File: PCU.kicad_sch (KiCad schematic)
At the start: 1 part, among them U2 EPC2152ENGRT

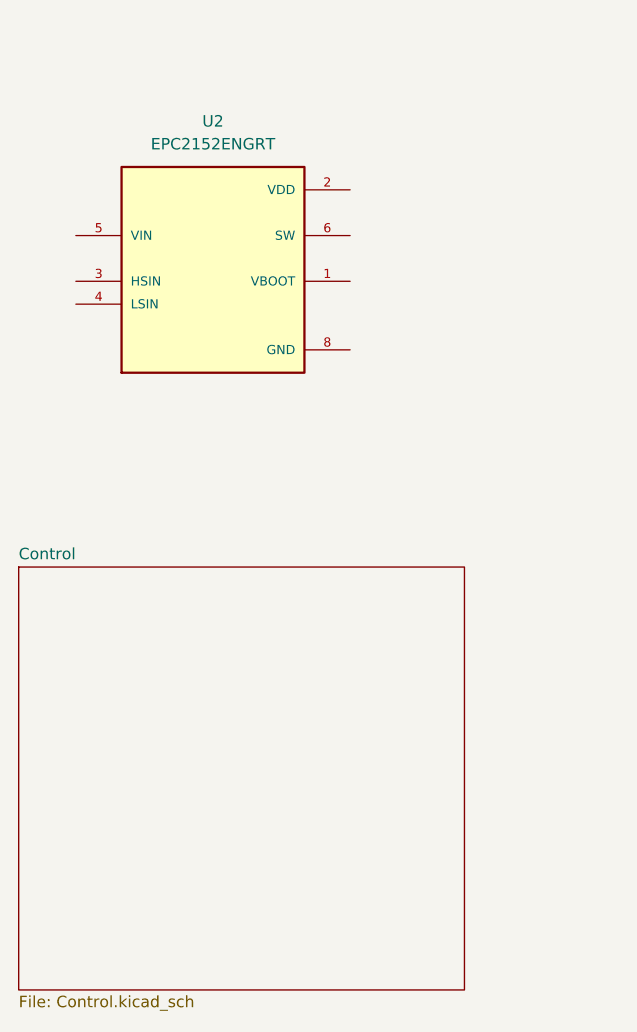
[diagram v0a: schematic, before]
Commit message: changed epc gan symbol
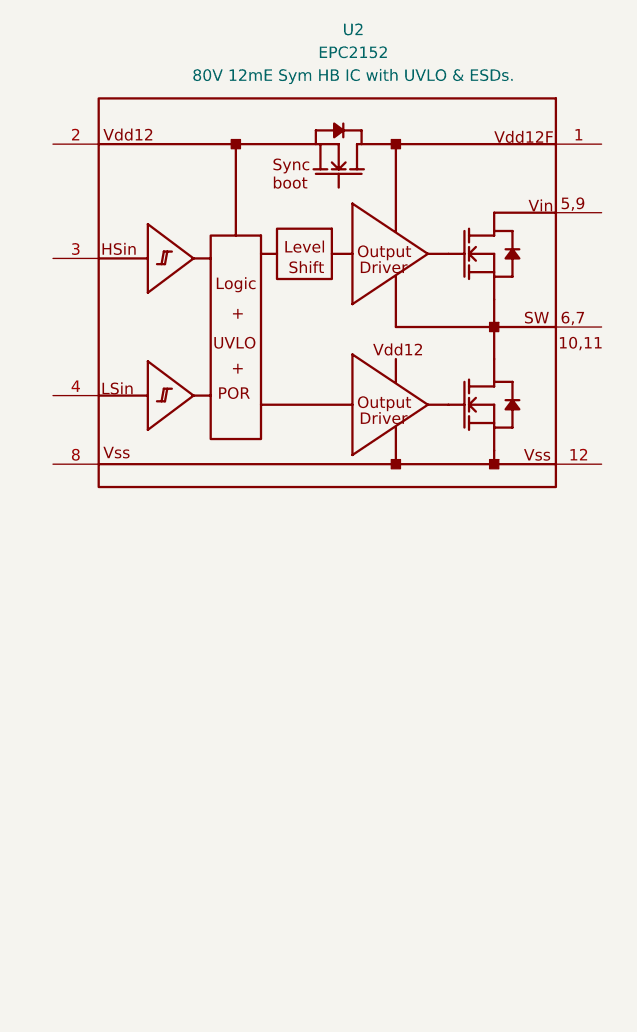
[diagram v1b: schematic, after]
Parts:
- removed U2: EPC2152ENGRT, PULSE_Library:VREG_EPC2152ENGRT, symbol PULSE_Library:EPC2152ENGRT
- added U2: EPC2152, PULSE_Library:D0122, symbol PULSE_Library:EPC2152
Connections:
- new net: U2.10 (SW), U2.11 (SW), U2.6 (SW), U2.7 (SW)
- new net: U2.5 (Vin), U2.9 (Vin)
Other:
- removed sheet Control
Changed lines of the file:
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@@
 	)
 	(symbol
-		(lib_id "PULSE_Library:EPC2152ENGRT")
-		(at 106.68 77.47 0)
+		(lib_id "PULSE_Library:EPC2152")
+		(at 93.98 102.87 0)
 		(unit 1)
 		(exclude_from_sim no)
@@
 		(fields_autoplaced yes)
 		(property "Reference" "U2"
-			(at 106.68 62.23 0)
+			(at 122.2761 52.07 0)
 			(effects
 				(font
@@
 			)
 		)
-		(property "Value" "EPC2152ENGRT"
-			(at 106.68 64.77 0)
+		(property "Value" "EPC2152"
+			(at 122.2761 54.61 0)
 			(effects
 				(font
@@
 			)
 		)
-		(property "Footprint" "PULSE_Library:VREG_EPC2152ENGRT"
-			(at 106.68 77.47 0)
-			(effects
-				(font
-					(size 1.27 1.27)
-				)
-				(justify bottom)
-				(hide yes)
-			)
-		)
-		(property "Datasheet" "https://epc-co.com/epc/portals/0/epc/documents/datasheets/EPC2152_datasheet.pdf"
-			(at 106.68 77.47 0)
+		(property "Footprint" "PULSE_Library:D0122"
+			(at 108.3564 56.2356 0)
 			(effects
 				(font
@@
 			)
 		)
-		(property "Description" "ePower™ Stage IC"
-			(at 106.68 77.47 0)
+		(property "Datasheet" ""
+			(at 93.98 102.87 0)
 			(effects
 				(font
@@
 			)
 		)
-		(property "MF" "EPC"
-			(at 106.68 77.47 0)
+		(property "Description" "80V 12mE Sym HB IC with UVLO & ESDs."
+			(at 122.2761 57.15 0)
 			(effects
 				(font
 					(size 1.27 1.27)
 				)
-				(justify bottom)
-				(hide yes)
 			)
 		)
-		(property "MAXIMUM_PACKAGE_HEIGHT" "0.842mm"
-			(at 106.68 77.47 0)
-			(effects
-				(font
-					(size 1.27 1.27)
-				)
-				(justify bottom)
-				(hide yes)
-			)
-		)
-		(property "Package" "WFLGA-12 EPC"
-			(at 106.68 77.47 0)
-			(effects
-				(font
-					(size 1.27 1.27)
-				)
-				(justify bottom)
-				(hide yes)
-			)
-		)
-		(property "Price" "None"
-			(at 106.68 77.47 0)
-			(effects
-				(font
-					(size 1.27 1.27)
-				)
-				(justify bottom)
-				(hide yes)
-			)
-		)
-		(property "Check_prices" "https://www.snapeda.com/parts/EPC2152ENGRT/EPC/view-part/?ref=eda"
-			(at 106.68 77.47 0)
-			(effects
-				(font
-					(size 1.27 1.27)
-				)
-				(justify bottom)
-				(hide yes)
-			)
-		)
-		(property "STANDARD" "Manufacturer Recommendations"
-			(at 106.68 77.47 0)
-			(effects
-				(font
-					(size 1.27 1.27)
-				)
-				(justify bottom)
-				(hide yes)
-			)
-		)
-		(property "PARTREV" "2.0"
-			(at 106.68 77.47 0)
-			(effects
-				(font
-					(size 1.27 1.27)
-				)
-				(justify bottom)
-				(hide yes)
-			)
-		)
-		(property "SnapEDA_Link" "https://www.snapeda.com/parts/EPC2152ENGRT/EPC/view-part/?ref=snap"
-			(at 106.68 77.47 0)
-			(effects
-				(font
-					(size 1.27 1.27)
-				)
-				(justify bottom)
-				(hide yes)
-			)
-		)
-		(property "MP" "EPC2152ENGRT"
-			(at 106.68 77.47 0)
-			(effects
-				(font
-					(size 1.27 1.27)
-				)
-				(justify bottom)
-				(hide yes)
-			)
-		)
-		(property "Description_1" "Half Bridge Driver Synchronous Buck Converters Gallium Nitride (GaN) FETs 12-LGA (3.85x2.59)"
-			(at 106.68 77.47 0)
-			(effects
-				(font
-					(size 1.27 1.27)
-				)
-				(justify bottom)
-				(hide yes)
-			)
-		)
-		(property "Availability" "In Stock"
-			(at 106.68 77.47 0)
-			(effects
-				(font
-					(size 1.27 1.27)
-				)
-				(justify bottom)
-				(hide yes)
-			)
-		)
-		(property "MANUFACTURER" "EPC"
-			(at 106.68 77.47 0)
-			(effects
-				(font
-					(size 1.27 1.27)
-				)
-				(justify bottom)
-				(hide yes)
-			)
-		)
-		(pin "12"
-		)
-		(pin "1"
-		)
-		(pin "7"
-		)
-		(pin "6"
-		)
-		(pin "11"
-		)
-		(pin "10"
-		)
-		(pin "2"
+		(pin "8"
 		)
 		(pin "4"
@@
 		(pin "3"
 		)
-		(pin "9"
+		(pin "2"
+		)
+		(pin "6"
+		)
+		(pin "12"
+		)
+		(pin "7"
+		)
+		(pin "1"
 		)
 		(pin "5"
 		)
-		(pin "8"
+		(pin "10"
+		)
+		(pin "9"
+		)
+		(pin "11"
 		)
 		(instances
@@
 				)
 			)
-		)
-	)
-	(sheet
-		(at 85.09 111.76)
-		(size 49.53 46.99)
-		(exclude_from_sim no)
-		(in_bom yes)
-		(on_board yes)
-		(dnp no)
-		(fields_autoplaced yes)
-		(stroke
-			(width 0.1524)
-			(type solid)
-		)
-		(fill
-			(color 0 0 0 0.0000)
-		)
-		(property "Sheetname" "Control"
-			(at 85.09 111.0484 0)
-			(effects
-				(font
-					(size 1.27 1.27)
-				)
-				(justify left bottom)
-			)
-		)
-		(property "Sheetfile" "Control.kicad_sch"
-			(at 85.09 159.3346 0)
-			(effects
-				(font
-					(size 1.27 1.27)
-				)
-				(justify left top)
-			)
-		)
-		(instances
-			(project "PULSE_ENG"
-				(path "/2de881bb-2e2a-47f9-96ed-b3393fa36b98/32fac869-3c72-4ec8-a514-1800b5db5371"
-					(page "5")
-				)
-			)

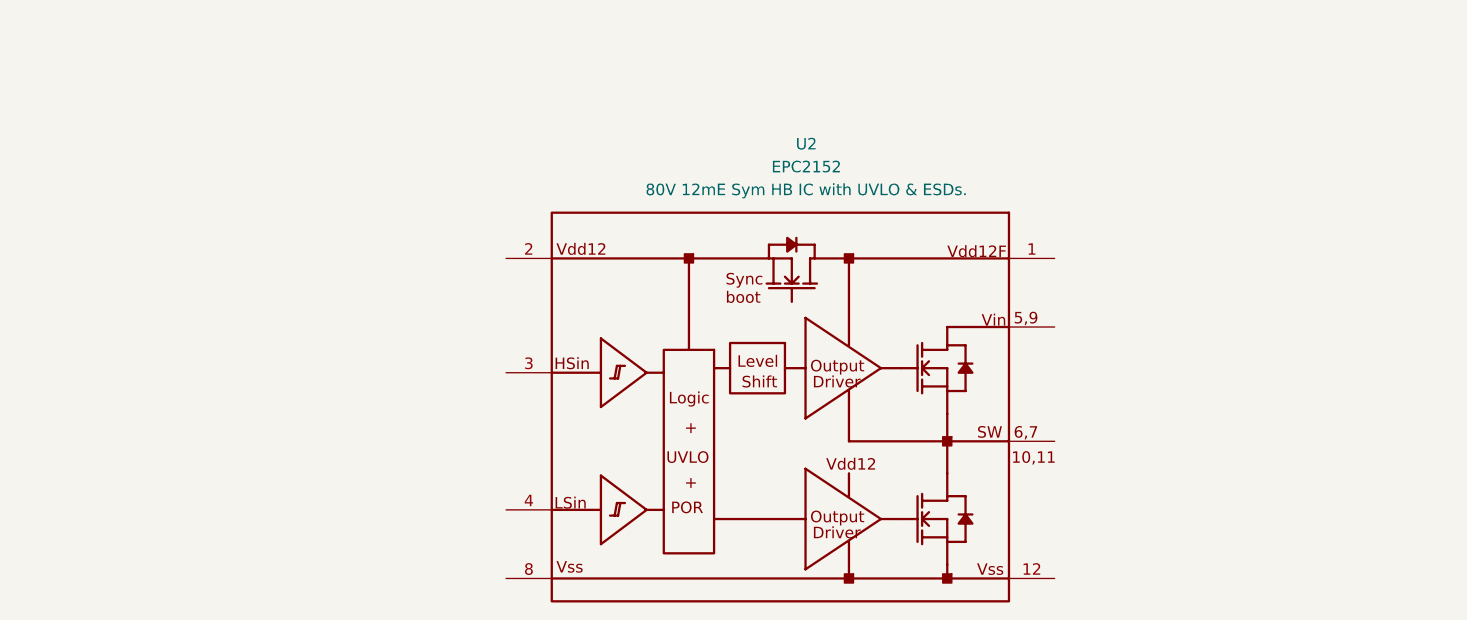
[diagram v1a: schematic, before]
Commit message: Add PCU buck converter section and notebook link
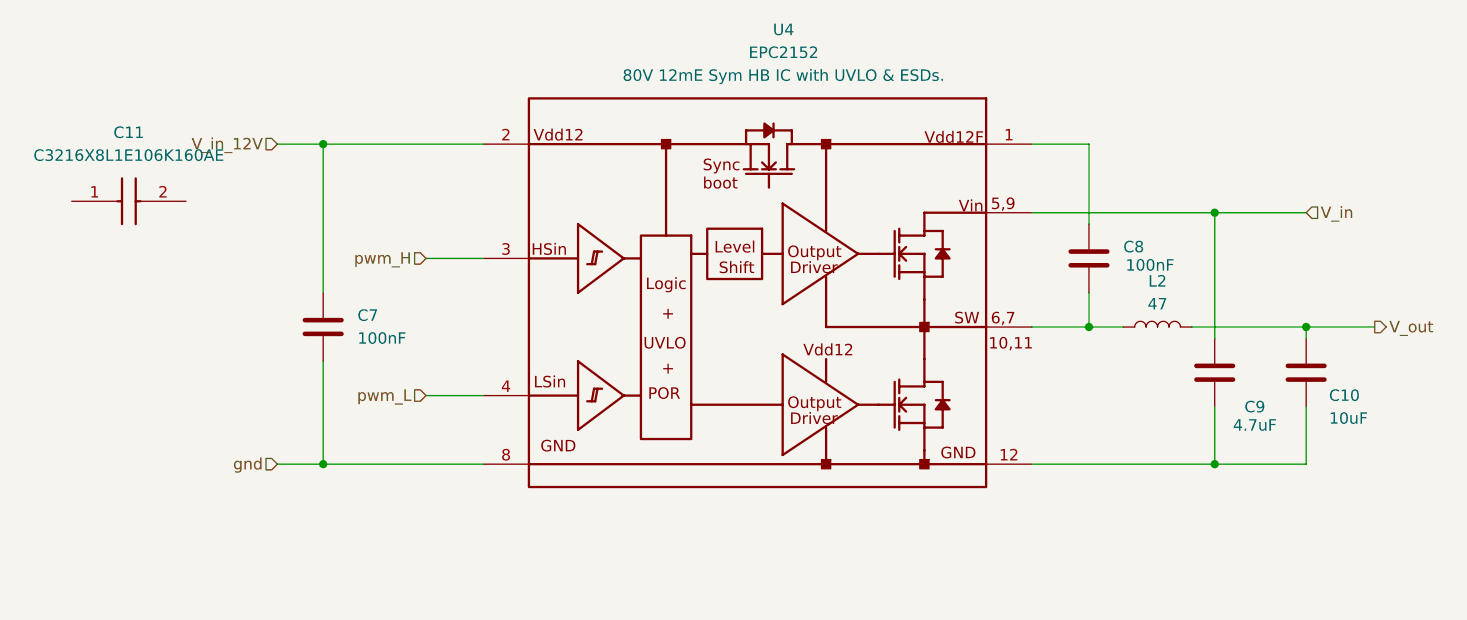
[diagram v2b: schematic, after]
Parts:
- removed U2: EPC2152, PULSE_Library:D0122, symbol PULSE_Library:EPC2152
- added C10: 10uF, symbol SamacSys_Parts:C
- added C11: C3216X8L1E106K160AE, CAPC3216X180N, symbol PULSE_Library:C3216X8L1E106K160AE
- added C7, C8: 100nF, symbol SamacSys_Parts:C
- added C9: 4.7uF, symbol SamacSys_Parts:C
- added L2: 47, symbol SamacSys_Parts:L
- added U4: EPC2152, EPC_FETs:D0122, symbol SamacSys_Parts:EPC2152
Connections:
- new net: C10.2, C9.2, U4.12 (Vss)
- new net: C8.1, U4.1 (Vdd12F)
- new net: C8.2, L2.1, U4.10 (SW), U4.11 (SW), U4.6 (SW), U4.7 (SW)
- new net V_in: C9.1, U4.5 (Vin), U4.9 (Vin)
- new net V_in_12V: C7.2, U4.2 (Vdd12)
- new net V_out: C10.1, L2.2
- new net gnd: C7.1, U4.8 (Vss)
- new net pwm_H: U4.3 (HSin)
- new net pwm_L: U4.4 (LSin)

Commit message: buck
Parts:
- removed C10: 10uF, symbol SamacSys_Parts:C
- removed C11: C3216X8L1E106K160AE, CAPC3216X180N, symbol PULSE_Library:C3216X8L1E106K160AE
- added C12: C3216X8L1E106K160AE, CAPC3216X180N, symbol PULSE_Library:C3216X8L1E106K160AE
- added Y1: AMDLA4020S-220MT, PULSE_Library:INDPM4440X200N, symbol PULSE_Library:AMDLA4020S-220MT
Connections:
- net V_out: now also C12.2
- net at C9.2, U4.12 (Vss): now also C12.1
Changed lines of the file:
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@@
+	)
+	(junction
+		(at 177.8 72.39)
+		(diameter 0)
+		(color 0 0 0 0)
 	)
 	(junction
@@
 		(color 0 0 0 0)
 	)
-	(junction
-		(at 177.8 72.39)
-		(diameter 0)
-		(color 0 0 0 0)
-	)
-	(wire
-		(pts
-			(xy 177.8 81.28) (xy 177.8 87.63)
+	(wire
+		(pts
+			(xy 177.8 72.39) (xy 185.42 72.39)
 		)
 		(stroke
@@
 	(wire
 		(pts
-			(xy 177.8 73.66) (xy 177.8 72.39)
-		)
-		(stroke
-			(width 0)
-			(type default)
-		)
-	)
-	(wire
-		(pts
 			(xy 153.67 72.39) (xy 157.48 72.39)
 		)
@@
 	(wire
 		(pts
-			(xy 177.8 72.39) (xy 185.42 72.39)
-		)
-		(stroke
-			(width 0)
-			(type default)
-		)
-	)
-	(wire
-		(pts
 			(xy 68.58 68.58) (xy 68.58 52.07)
 		)
@@
 		(pts
 			(xy 153.67 52.07) (xy 153.67 60.96)
+		)
+		(stroke
+			(width 0)
+			(type default)
+		)
+	)
+	(wire
+		(pts
+			(xy 177.8 74.93) (xy 177.8 72.39)
 		)
 		(stroke
@@
 	)
 	(symbol
-		(lib_id "SamacSys_Parts:C")
-		(at 177.8 77.47 0)
-		(unit 1)
-		(exclude_from_sim no)
-		(in_bom yes)
-		(on_board yes)
-		(dnp no)
-		(property "Reference" "C10"
-			(at 180.34 80.01 0)
-			(effects
-				(font
-					(size 1.27 1.27)
-				)
-				(justify left)
-			)
-		)
-		(property "Value" "10uF"
-			(at 180.34 82.55 0)
-			(effects
-				(font
-					(size 1.27 1.27)
-				)
-				(justify left)
-			)
-		)
-		(property "Footprint" ""
-			(at 178.7652 81.28 0)
-			(effects
-				(font
-					(size 1.27 1.27)
-				)
-				(hide yes)
-			)
-		)
-		(property "Datasheet" "~"
-			(at 177.8 77.47 0)
-			(effects
-				(font
-					(size 1.27 1.27)
-				)
-				(hide yes)
-			)
-		)
-		(property "Description" "Unpolarized capacitor"
-			(at 177.8 77.47 0)
-			(effects
-				(font
-					(size 1.27 1.27)
-				)
-				(hide yes)
-			)
-		)
-		(pin "2"
-		)
-		(pin "1"
-		)
-		(instances
-			(project "PULSE_ENG"
-				(path "/2de881bb-2e2a-47f9-96ed-b3393fa36b98/32fac869-3c72-4ec8-a514-1800b5db5371"
-					(reference "C10")
-					(unit 1)
-				)
-			)
-		)
-	)
-	(symbol
 		(lib_id "PULSE_Library:C3216X8L1E106K160AE")
-		(at 40.64 58.42 0)
+		(at 177.8 87.63 90)
 		(unit 1)
 		(exclude_from_sim no)
@@
 		(dnp no)
 		(fields_autoplaced yes)
-		(property "Reference" "C11"
-			(at 46.99 50.8 0)
-			(effects
-				(font
-					(size 1.27 1.27)
-				)
+		(property "Reference" "C12"
+			(at 181.61 80.0099 90)
+			(effects
+				(font
+					(size 1.27 1.27)
+				)
+				(justify right)
 			)
 		)
 		(property "Value" "C3216X8L1E106K160AE"
-			(at 46.99 53.34 0)
-			(effects
-				(font
-					(size 1.27 1.27)
-				)
+			(at 181.61 82.5499 90)
+			(effects
+				(font
+					(size 1.27 1.27)
+				)
+				(justify right)
 			)
 		)
 		(property "Footprint" "CAPC3216X180N"
-			(at 49.53 154.61 0)
+			(at 273.99 78.74 0)
 			(effects
 				(font
@@
 		)
 		(property "Datasheet" "https://product.tdk.com/info/en/catalog/datasheets/mlcc_commercial_midvoltage_en.pdf"
-			(at 49.53 254.61 0)
+			(at 373.99 78.74 0)
 			(effects
 				(font
@@
 		)
 		(property "Description" "MULTILAYER CERAMIC CHIP CAPACITORS, 3216, Commercial grade, general (Up to 75V)"
-			(at 40.64 58.42 0)
+			(at 177.8 87.63 0)
 			(effects
 				(font
@@
 		)
 		(property "Height" "1.8"
-			(at 49.53 454.61 0)
+			(at 573.99 78.74 0)
 			(effects
 				(font
@@
 		)
 		(property "Mouser Part Number" "810-C3216X8L106K160E"
-			(at 49.53 554.61 0)
+			(at 673.99 78.74 0)
 			(effects
 				(font
@@
 		)
 		(property "Mouser Price/Stock" "https://www.mouser.co.uk/ProductDetail/TDK/C3216X8L1E106K160AE?qs=P1JMDcb91o4c0as04x%252BvyQ%3D%3D"
-			(at 49.53 654.61 0)
+			(at 773.99 78.74 0)
 			(effects
 				(font
@@
 		)
 		(property "Manufacturer_Name" "TDK"
-			(at 49.53 754.61 0)
+			(at 873.99 78.74 0)
 			(effects
 				(font
@@
 		)
 		(property "Manufacturer_Part_Number" "C3216X8L1E106K160AE"
-			(at 49.53 854.61 0)
+			(at 973.99 78.74 0)
 			(effects
 				(font
@@
 		)
 		(instances
-			(project ""
+			(project "PULSE_ENG"
 				(path "/2de881bb-2e2a-47f9-96ed-b3393fa36b98/32fac869-3c72-4ec8-a514-1800b5db5371"
-					(reference "C11")
+					(reference "C12")
 					(unit 1)
 				)
@@
 					(unit 1)
 				)
+			)
+		)
+	)
+	(symbol
+		(lib_id "PULSE_Library:AMDLA4020S-220MT")
+		(at 31.75 36.83 0)
+		(unit 1)
+		(exclude_from_sim no)
+		(in_bom yes)
+		(on_board yes)
+		(dnp no)
+		(fields_autoplaced yes)
+		(property "Reference" "Y1"
+			(at 36.83 27.94 0)
+			(effects
+				(font
+					(size 1.27 1.27)
+				)
+			)
+		)
+		(property "Value" "AMDLA4020S-220MT"
+			(at 36.83 30.48 0)
+			(effects
+				(font
+					(size 1.27 1.27)
+				)
+			)
+		)
+		(property "Footprint" "PULSE_Library:INDPM4440X200N"
+			(at 40.64 133.02 0)
+			(effects
+				(font
+					(size 1.27 1.27)
+				)
+				(justify left top)
+				(hide yes)
+			)
+		)
+		(property "Datasheet" "https://abracon.com/datasheets/AMDLA4020S.pdf"
+			(at 40.64 233.02 0)
+			(effects
+				(font
+					(size 1.27 1.27)
+				)
+				(justify left top)
+				(hide yes)
+			)
+		)
+		(property "Description" "FIXED IND 22UH 1.2A 320MOHM SMD"
+			(at 31.75 36.83 0)
+			(effects
+				(font
+					(size 1.27 1.27)
+				)
+				(hide yes)
+			)
+		)
+		(property "Height" "2"
+			(at 40.64 433.02 0)
+			(effects
+				(font
+					(size 1.27 1.27)
+				)
+				(justify left top)
+				(hide yes)
+			)
+		)
+		(property "Mouser Part Number" "815-AMDLA4020S-220MT"
+			(at 40.64 533.02 0)
+			(effects
+				(font
+					(size 1.27 1.27)
+				)
+				(justify left top)
+				(hide yes)
+			)
+		)
+		(property "Mouser Price/Stock" "https://www.mouser.co.uk/ProductDetail/ABRACON/AMDLA4020S-220MT?qs=DPoM0jnrROWKifSgrOC28g%3D%3D"
+			(at 40.64 633.02 0)
+			(effects
+				(font
+					(size 1.27 1.27)
+				)
+				(justify left top)
+				(hide yes)
+			)
+		)
+		(property "Manufacturer_Name" "ABRACON"
+			(at 40.64 733.02 0)
+			(effects
+				(font
+					(size 1.27 1.27)
+				)
+				(justify left top)
+				(hide yes)
+			)
+		)
+		(property "Manufacturer_Part_Number" "AMDLA4020S-220MT"
+			(at 40.64 833.02 0)
+			(effects
+				(font
+					(size 1.27 1.27)
+				)
+				(justify left top)
+				(hide yes)
+			)
+		)
+		(pin "1"
+		)
+		(pin "2"
+		)
+		(instances
+			(project ""
+				(path "/2de881bb-2e2a-47f9-96ed-b3393fa36b98/32fac869-3c72-4ec8-a514-1800b5db5371"
+					(reference "Y1")
+					(unit 1)
+				)

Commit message: Adjusting footprints of components
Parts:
- C12: footprint CAPC3216X180N -> PULSE_Library:CAPC3216X180N
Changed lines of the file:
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@@
 			)
 		)
-		(property "Footprint" "CAPC3216X180N"
+		(property "Footprint" "PULSE_Library:CAPC3216X180N"
 			(at 273.99 78.74 0)
 			(effects

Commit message: Big final PCU PCB design
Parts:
- added J11: Screw_Terminal_01x01, TerminalBlock_Phoenix:TerminalBlock_Phoenix_MKDS-1,5-2-5.08_1x02_P5.08mm_Horizontal, symbol Connector:Screw_Terminal_01x01
- added TP2: 12Vin_buck, TestPoint:TestPoint_Pad_D2.0mm, symbol Connector:TestPoint_Probe
- added TP5: PWM_H, TestPoint:TestPoint_Pad_D2.0mm, symbol Connector:TestPoint_Probe
- added TP6: PWM_L, TestPoint:TestPoint_Pad_D2.0mm, symbol Connector:TestPoint_Probe
- added TP7: Buck_out, TestPoint:TestPoint_Pad_D2.0mm, symbol Connector:TestPoint_2Pole
- C7, C8, C9: footprint (none) -> Capacitor_SMD:C_0201_0603Metric
- L2: footprint (none) -> Inductor_THT:L_Axial_L7.0mm_D3.3mm_P10.16mm_Horizontal_Fastron_MICC
- U4: footprint EPC_FETs:D0122 -> PULSE_Library:VREG_EPC2152ENGRT
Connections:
- net V_in_12V: now also TP2.1
- net V_out: now also J11.1 (Pin_1), TP7.1
- net pwm_H: now also TP5.1
- net pwm_L: now also TP6.1
- net at C12.1, C9.2, U4.12 (Vss): now also TP7.2
- net gnd renamed GROUND
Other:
- moved on the sheet: C7
